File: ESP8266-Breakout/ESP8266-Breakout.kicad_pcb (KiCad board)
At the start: 2 copper layers, 26.2 x 40 mm, 23 parts, among them J101 Conn_01x08_Female, J102 Conn_01x08_Female, J103 FTDI, SW101 Flash, SW102 RST, U102 ESP-12F

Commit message: New version completed, shematic + pcb wired
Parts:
- removed C105: 100nF, Capacitor_SMD:C_1206_3216Metric_Pad1.33x1.80mm_HandSolder
- removed C106: 10uF, Capacitor_SMD:C_1206_3216Metric_Pad1.33x1.80mm_HandSolder
- removed D101: TX, LED_SMD:LED_0603_1608Metric_Pad1.05x0.95mm_HandSolder
- removed D102: RX, LED_SMD:LED_0603_1608Metric_Pad1.05x0.95mm_HandSolder
- removed J103: FTDI, Connector_PinHeader_2.54mm:PinHeader_1x06_P2.54mm_Vertical
- removed JP101: Power, Jumper:SolderJumper-2_P1.3mm_Bridged_RoundedPad1.0x1.5mm
- removed R101, R102, R103, R105, R106: 10K, Resistor_SMD:R_0603_1608Metric_Pad0.98x0.95mm_HandSolder
- removed R104, R107: 15, Resistor_SMD:R_0805_2012Metric_Pad1.20x1.40mm_HandSolder
- removed SW101: Flash, Button_Switch_SMD:SW_SPST_CK_RS282G05A3
- removed SW102: RST, Button_Switch_SMD:SW_SPST_CK_RS282G05A3
- removed U102: ESP-12F, RF_Module:ESP-12E
- removed Ue: AMS1117-3.3, Package_TO_SOT_SMD:SOT-223-3_TabPin2
- added C501: 0.1uF, Capacitor_SMD:C_0603_1608Metric_Pad1.08x0.95mm_HandSolder, F.Cu at (142.2, 98.4)
- added C502: 47uF, Capacitor_SMD:C_1206_3216Metric_Pad1.33x1.80mm_HandSolder, F.Cu at (152.2, 97.6)
- added D501: TX, LED_SMD:LED_0603_1608Metric_Pad1.05x0.95mm_HandSolder, F.Cu at (141.2, 68.3)
- added D502: RX, LED_SMD:LED_0603_1608Metric_Pad1.05x0.95mm_HandSolder, F.Cu at (163.1, 68.5)
- added J501: FTDI, Connector_PinHeader_2.54mm:PinHeader_1x06_P2.54mm_Vertical, F.Cu at (158.6, 93.2)
- added JP501: Power, Jumper:SolderJumper-2_P1.3mm_Bridged_RoundedPad1.0x1.5mm, B.Cu at (152.7, 86.3)
- added R501: 10K, Resistor_SMD:R_0603_1608Metric_Pad0.98x0.95mm_HandSolder, F.Cu at (159.1, 98.4)
- added R502: 10K, Resistor_SMD:R_0603_1608Metric_Pad0.98x0.95mm_HandSolder, F.Cu at (145.3, 98.4)
- added R503: 10K, Resistor_SMD:R_0603_1608Metric_Pad0.98x0.95mm_HandSolder, F.Cu at (143.8, 98.4)
- added R504: 15, Resistor_SMD:R_0805_2012Metric_Pad1.20x1.40mm_HandSolder, F.Cu at (141.2, 71.1)
- added R505: 10K, Resistor_SMD:R_0603_1608Metric_Pad0.98x0.95mm_HandSolder, F.Cu at (160.7, 98.4)
- added R506: 10K, Resistor_SMD:R_0603_1608Metric_Pad0.98x0.95mm_HandSolder, F.Cu at (162.3, 98.4)
- added R507: 15, Resistor_SMD:R_0805_2012Metric_Pad1.20x1.40mm_HandSolder, F.Cu at (163.3, 71.2)
- added SW501: Flash, Button_Switch_SMD:SW_SPST_CK_RS282G05A3, F.Cu at (159.9, 102.2)
- added SW502: RST, Button_Switch_SMD:SW_SPST_CK_RS282G05A3, F.Cu at (144.2, 102.2)
- added TP101: TestPoint, TestPoint:TestPoint_Pad_D3.0mm, B.Cu at (144.1, 102.2)
- added TP102: TestPoint, TestPoint:TestPoint_Pad_D3.0mm, B.Cu at (160.0, 102.2)
- added U101: AMS1117-3.3, Package_TO_SOT_SMD:SOT-223-3_TabPin2, B.Cu at (152.7, 79.5)
- added U501: ESP-12F, RF_Module:ESP-12E, F.Cu at (152.2, 77.7)
- C102: value 0.1uF -> 100nF; footprint Capacitor_SMD:C_0603_1608Metric_Pad1.08x0.95mm_HandSolder -> Capacitor_SMD:C_1206_3216Metric_Pad1.33x1.80mm_HandSolder
- C104: value 47uF -> 10uF
- J101, J102: value Conn_01x08_Female -> Conn_01x09_Female; footprint Connector_PinSocket_2.54mm:PinSocket_1x08_P2.54mm_Vertical -> Custom:PinHeader_1x09_P2.54mm_Vertical_without_silkscrean
- moved J102 24.3 mm to (163.6, 74.9), turned to 0 degrees
- moved C103 9.34 mm to (154.7, 97.6)
- moved C104 9.14 mm to (157.1, 97.6)
- moved C102 9.00 mm to (147.3, 97.6), turned to 270 degrees
- moved C101 8.71 mm to (149.8, 97.6)
- moved J101 6.62 mm to (140.6, 74.9)
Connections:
- C102 pad 1: +3V3 -> +5V
- C103 pad 1: +5V -> +3V3
- J101 pad 1: /~RST -> /RST
- J102 pad 1: GND -> /GPIO1
- J102 pad 2: /GPIO15 -> /GPIO3
- J102 pad 3: /GPIO2 -> /GPIO5
- J102 pad 4: /~FLASH -> /GPIO4
- J102 pad 5: /GPIO4 -> /GPIO0
- J102 pad 6: /GPIO5 -> /GPIO2
- J102 pad 7: /RX -> /GPIO15
- J102 pad 8: /TX -> GND
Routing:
- net +3V3: track 0.00 -> 62.5 mm, vias 0 -> 1
- net /GPIO1: track 0.00 -> 45.1 mm
- net +5V: track 0.00 -> 41.4 mm, vias 0 -> 1
- net /RST: track 0.00 -> 38.6 mm, vias 0 -> 1
- net /GPIO3: track 0.00 -> 32.1 mm, vias 0 -> 2
- net /GPIO0: track 0.00 -> 27.1 mm, vias 0 -> 2
- net /EN: track 0.00 -> 23.5 mm, vias 0 -> 1
- net /GPIO2: track 0.00 -> 16.9 mm, vias 0 -> 1
- net /GPIO15: track 0.00 -> 14.5 mm, vias 0 -> 1
- net /GPIO10: track 0.00 -> 14.4 mm
- net Net-(J501-Pad4): track 0.00 -> 7.05 mm
- net /GPIO13: track 0.00 -> 5.95 mm
- net /GPIO12: track 0.00 -> 5.41 mm
- net /GPIO14: track 0.00 -> 5.18 mm
- net /GPIO16: track 0.00 -> 4.96 mm
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- added copper zone on B.Cu, net GND
- removed copper zone on B.Cu, net (none)
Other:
- board size 26.2 x 40 mm -> 25.6 x 39.1 mm
- board text added: "0"
- board text added: "10"
- board text added: "12"
- board text added: "13"
- board text added: "14"
- board text added: "15"
- board text added: "16"
- board text added: "2"
- board text added: "3v3"
- board text added: "4"
- board text added: "5"
- board text added: "5V"
- board text added: "AD"
- board text added: "EN"
- board text added: "Gnd"
- board text added: "RS"
- board text added: "RX"
- board text added: "TX"

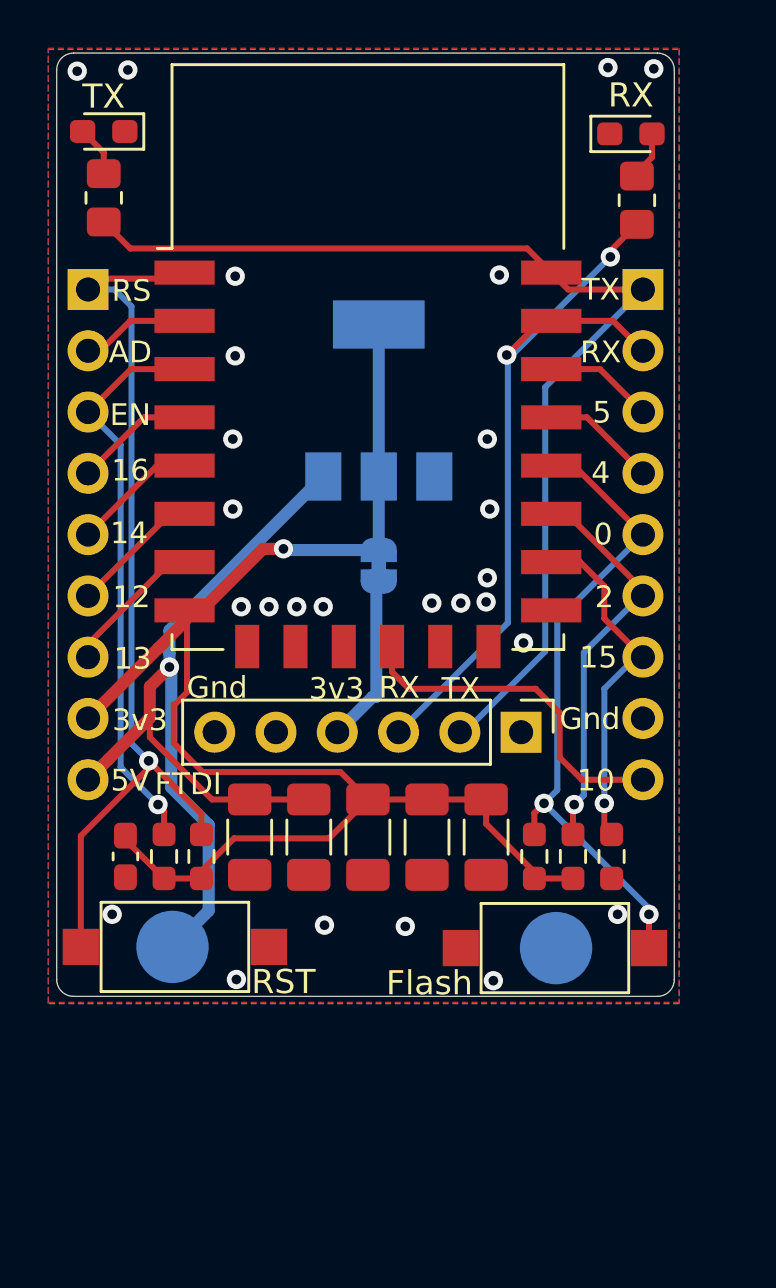
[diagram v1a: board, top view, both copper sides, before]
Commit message: Single and panel board views added
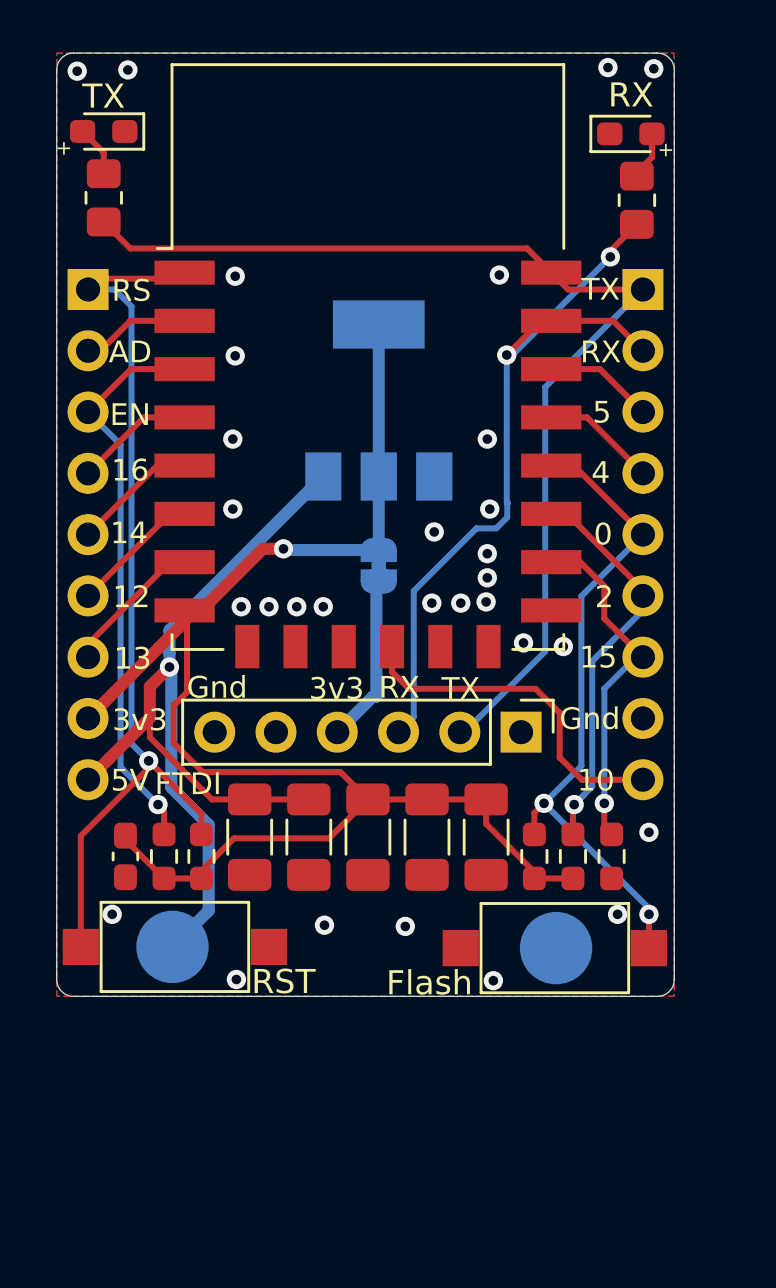
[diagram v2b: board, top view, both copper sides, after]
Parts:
- added REF**: KiCad-Logo_5mm_SilkScreen, Symbol:KiCad-Logo_5mm_SilkScreen, B.Cu at (152.1, 68.8)
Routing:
- net GND: vias 26 -> 30
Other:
- board text added: "+"
- board text added: "AMS1117"
- board text added: "ESP8266 Breakout Board"

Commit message: Release 2
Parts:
- JP501: footprint Jumper:SolderJumper-2_P1.3mm_Bridged_RoundedPad1.0x1.5mm -> Jumper:SolderJumper-2_P1.3mm_Open_RoundedPad1.0x1.5mm
